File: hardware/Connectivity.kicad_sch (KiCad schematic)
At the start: 20 parts, among them U1 MCP2542FD-E/MF, U6 MCP2542FD-E/MF, U7 MCP2542FD-E/MF

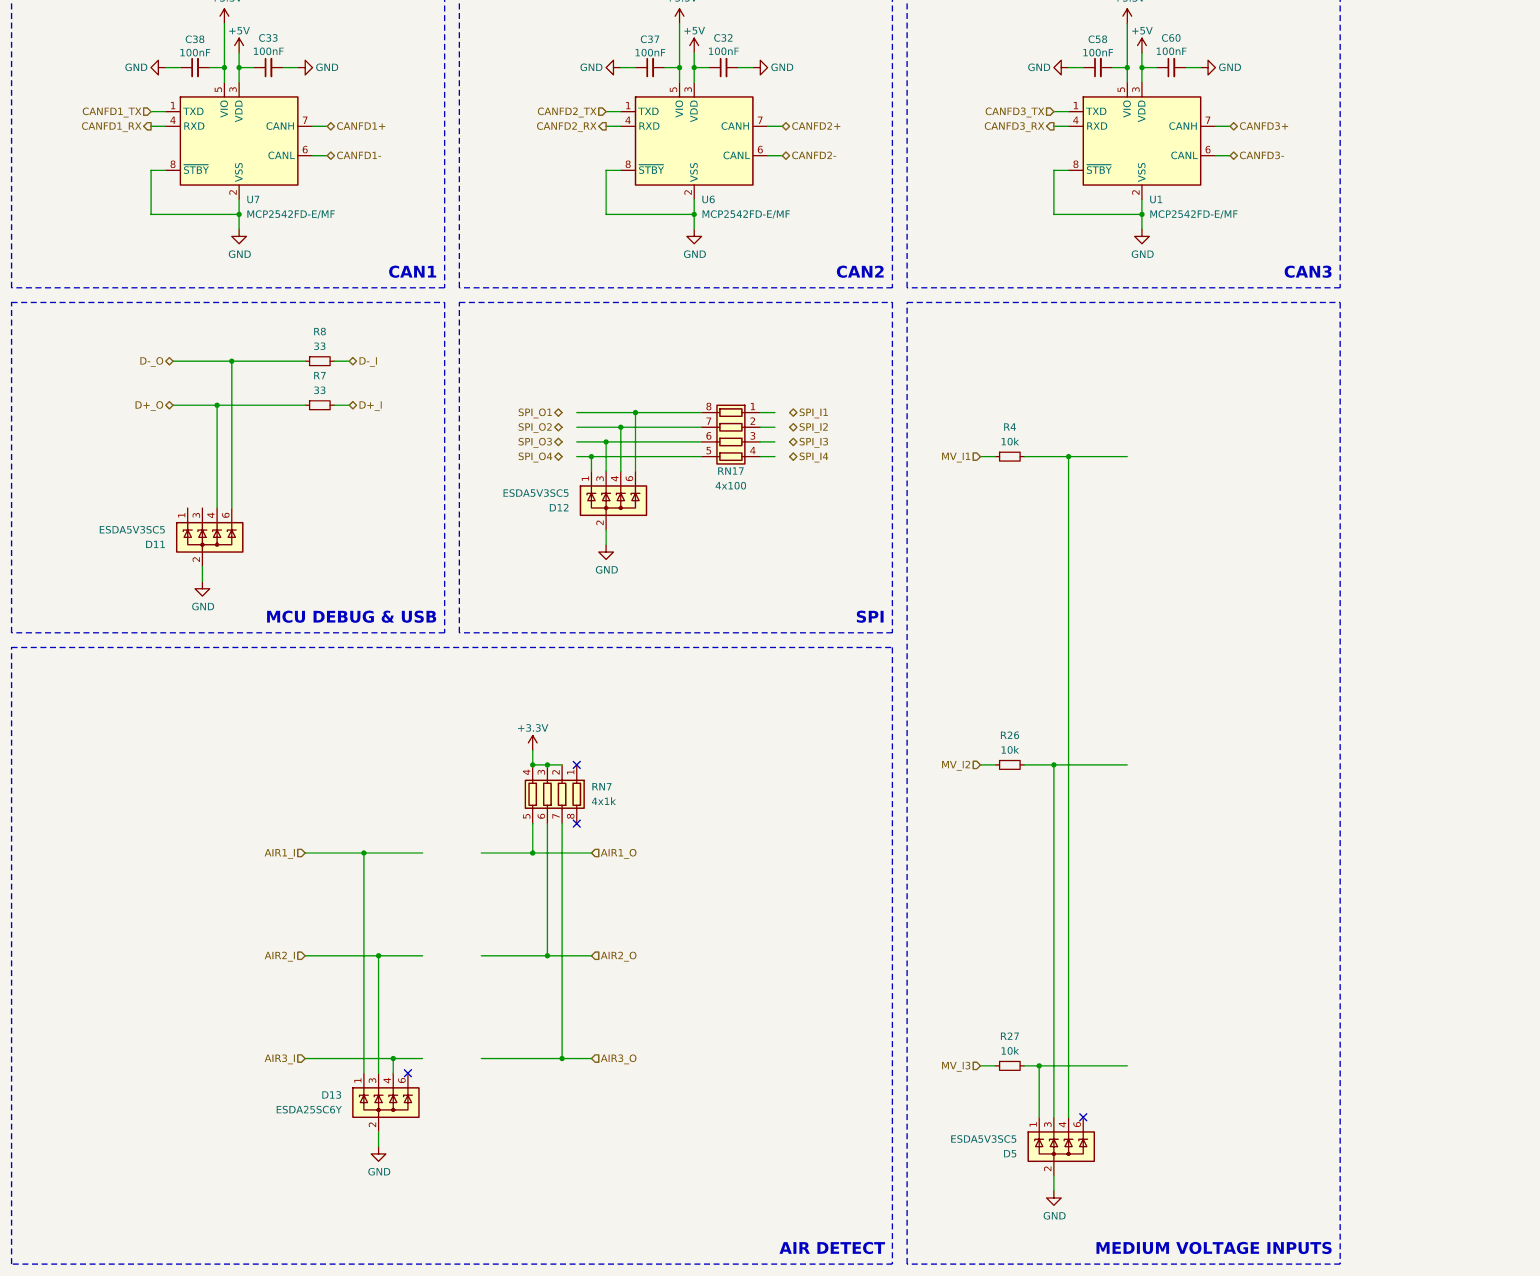
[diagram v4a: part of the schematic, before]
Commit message: inductors 3d models fix, smaller relay (same series as the one from IMD), other + sync
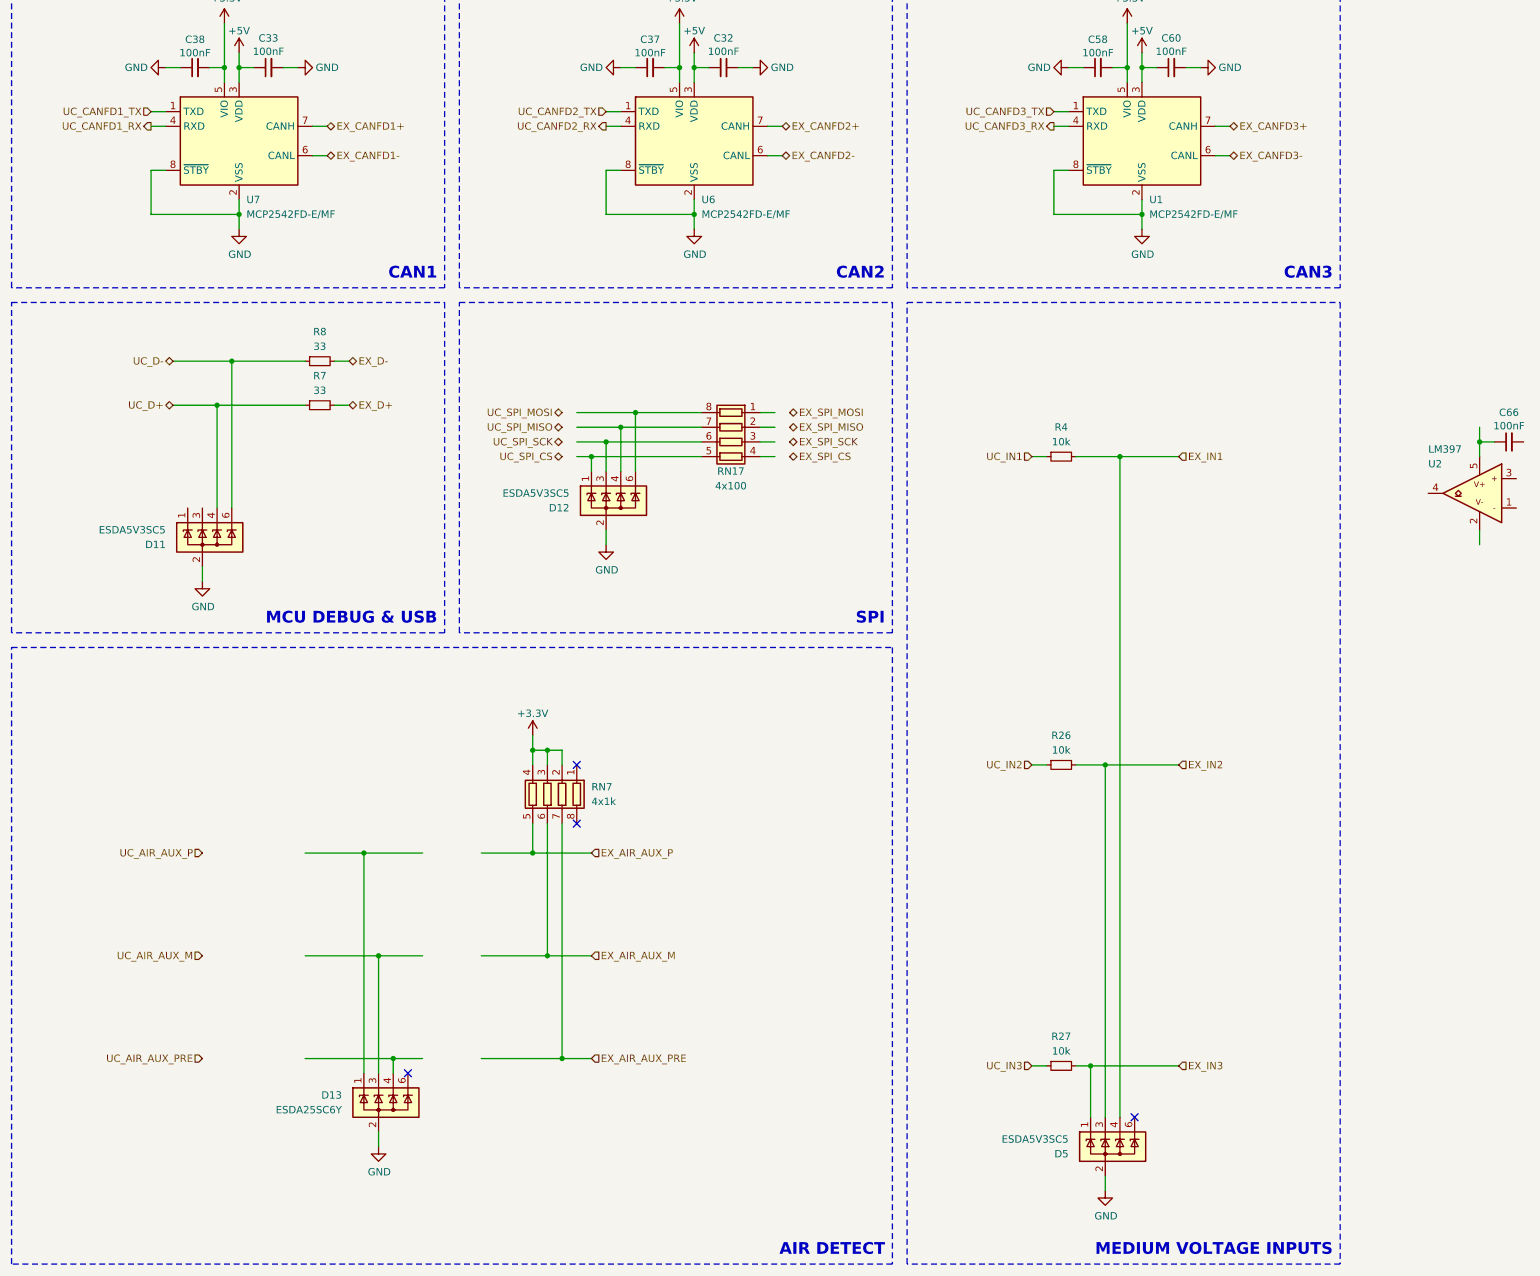
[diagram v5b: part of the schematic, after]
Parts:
- added C66: 100nF, Capacitor_SMD:C_0603_1608Metric, symbol Device:C_Small
- added U2: LM397, Package_TO_SOT_SMD:SOT-23-5, symbol Comparator:LM397
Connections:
- net EX_IN3: now reaches D5.1 (A), R27.2
- net EX_IN1: now reaches D5.4 (A), R4.2
- net EX_IN2: now reaches D5.3 (A), R26.2
- net AIR1_I: no longer names the net of D13.1 (A)
- net AIR1_O renamed EX_AIR_AUX_P
- net AIR2_I: no longer names the net of D13.3 (A)
- net AIR2_O renamed EX_AIR_AUX_M
- net AIR3_I: no longer names the net of D13.4 (A)
- net AIR3_O renamed EX_AIR_AUX_PRE
- net CANFD1+ renamed EX_CANFD1+
- net CANFD1- renamed EX_CANFD1-
- net CANFD1_RX renamed UC_CANFD1_RX
- net CANFD1_TX renamed UC_CANFD1_TX
- net CANFD2+ renamed EX_CANFD2+
- net CANFD2- renamed EX_CANFD2-
- net CANFD2_RX renamed UC_CANFD2_RX
- net CANFD2_TX renamed UC_CANFD2_TX
- net CANFD3+ renamed EX_CANFD3+
- net CANFD3- renamed EX_CANFD3-
- net CANFD3_RX renamed UC_CANFD3_RX
- net CANFD3_TX renamed UC_CANFD3_TX
- net D+_I renamed EX_D+
- net D+_O renamed UC_D+
- net D-_I renamed EX_D-
- net D-_O renamed UC_D-
- net MV_I1 renamed UC_IN1
- net MV_I2 renamed UC_IN2
- net MV_I3 renamed UC_IN3
- new net: C66.1, U2.5
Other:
- moved on the sheet: D5, R26, R27, R4

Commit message: all but the communications sections done
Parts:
- removed D13: ESDA25SC6Y, Package_TO_SOT_SMD:SOT-23-6, symbol Power_Protection:ESDA5V3SC5
- removed D5: ESDA5V3SC5, Package_TO_SOT_SMD:SOT-23-6, symbol Power_Protection:ESDA5V3SC5
- removed R27, R4: 10k, Resistor_SMD:R_0603_1608Metric, symbol Device:R_Small
- removed RN17: 4x100, Resistor_SMD:R_Array_Convex_4x0603, symbol Device:R_Pack04
- removed RN7: 4x1k, Resistor_SMD:R_Array_Convex_4x0603, symbol Device:R_Pack04
- added C5, C72, C74, C76: 10nF, Capacitor_SMD:C_0603_1608Metric, symbol Device:C_Small
- added C50, C71, C73, C75, C77: 100nF, Capacitor_SMD:C_0603_1608Metric, symbol Device:C_Small
- added R15, R17, R32, R38, R39, R40, R41, R70, R71, R72, R73, R77, R78, R79, R80, R84, R85, R86, R87: 10k, Resistor_SMD:R_0603_1608Metric, symbol Device:R_Small
- added R33, R35, R42, R43, R68, R69, R74, R75, R76, R81, R82, R83, R88, R89, R90: TBD, Resistor_SMD:R_0603_1608Metric, symbol Device:R_Small
- added R49, R50, R51, R52: 33, Resistor_SMD:R_0603_1608Metric, symbol Device:R_Small
- added U11, U5, U8, U9: LM397, Package_TO_SOT_SMD:SOT-23-5, symbol Comparator:LM397
- added unit 2 of U2
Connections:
- net +3.3V: now also R26.1, R15.1, R38.1, R40.1, R70.1, R72.1, R77.1, R79.1, R84.1, R86.1
- net EX_AIR_AUX_M: now also R83.2
- net EX_AIR_AUX_P: now also R90.2
- net EX_AIR_AUX_PRE: now also R76.2
- net EX_IN1: now also R42.2
- net EX_IN2: now also R33.2; no longer R26.2
- net EX_SPI_CS: now also R50.2
- net EX_SPI_MISO: now also R51.2
- net EX_SPI_MOSI: now also R52.2
- net EX_SPI_SCK: now also R49.2
- net GND: now also C66.2, C5.2, C50.2, C71.2, C72.2, C73.2, C74.2, C75.2, C76.2, C77.2, R32.2, R35.2, R41.2, R43.2, R73.2, R75.2, R80.2, R82.2, R87.2, R89.2, U11.2 (VSS), U2.2 (VSS), U5.2 (VSS), U8.2 (VSS), U9.2 (VSS)
- net UC_AIR_AUX_M: now also R77.2, R78.2, U9.4
- net UC_AIR_AUX_P: now also R84.2, R85.2, U11.4
- net UC_AIR_AUX_PRE: now also R70.2, R71.2, U8.4
- net UC_IN1: now also R38.2, R39.2, U5.4
- net UC_IN2: now also U2.4, R15.2, R17.2; no longer R26.1
- net UC_SPI_CS: now also D12.1 (A), R50.1
- net UC_SPI_MISO: now also D12.4 (A), R51.1
- net UC_SPI_MOSI: now also D12.6 (A), R52.1
- net UC_SPI_SCK: now also D12.3 (A), R49.1
- net +24V: now reaches C66.1
- net +24V: now also C71.1, C73.1, C75.1, C77.1, R68.1, R69.1, R74.1, R81.1, R88.1, U11.5 (VDD), U2.5 (VDD), U5.5 (VDD), U8.5 (VDD), U9.5 (VDD); no longer U2.5
- net at U2.1: now also R26.2, R17.1, R32.1
- net at U2.3: now also C5.1, R33.1, R35.1, R69.2
- new net: R78.1, R79.2, R80.1, U9.1
- new net: R71.1, R72.2, R73.1, U8.1
- new net: C50.1, R42.1, R43.1, R68.2, U5.3
- new net: C72.1, R74.2, R75.1, R76.1, U8.3
- new net: C74.1, R81.2, R82.1, R83.1, U9.3
- new net: R39.1, R40.2, R41.1, U5.1
- new net: R85.1, R86.2, R87.1, U11.1
- new net: C76.1, R88.2, R89.1, R90.1, U11.3
- no-connect marks 4 -> 0
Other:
- moved on the sheet: C32, C33, C37, C38, C58, C60, D11, D12, R7, R8, U1, U6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

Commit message: sync
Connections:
- no-connect marks 0 -> 2
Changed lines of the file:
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@@
 		(color 0 0 0 0)
+	)
+	(no_connect
+		(at 360.68 146.05)
+	)
+	(no_connect
+		(at 363.22 146.05)
 	)
 	(wire

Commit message: sync
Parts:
- C32, C33, C37, C38, C50, C58, C60, C66, C71, C73, C75, C77: Mouser Price/Stock (none) -> https://www.mouser.pl/ProductDetail/KEMET/C0603C104J3RACTU?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
- R15, R17, R26, R32, R38, R39, R40, R41, R70, R71, R72, R73, R77, R78, R79, R80, R84, R85, R86, R87: Mouser Price/Stock (none) -> https://www.mouser.pl/ProductDetail/YAGEO/RT0603DRE07100KL?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
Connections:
- net EI2: now reaches C5.1, R33.1, R35.1, R69.2, U2.3
- net EI1: now reaches C50.1, R42.1, R43.1, R68.2, U5.3
- net EAAE: now reaches C72.1, R74.2, R75.1, R76.1, U8.3
- net EAAM: now reaches C74.1, R81.2, R82.1, R83.1, U9.3
- net EAAP: now reaches C76.1, R88.2, R89.1, R90.1, U11.3
